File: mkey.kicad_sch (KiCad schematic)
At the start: 161 parts, among them J1 USB_C_REP_2.0, SW1 SW_Push, SW2 SW_Push, U1 ESP32-S3-WROOM-1, U5 SY8088

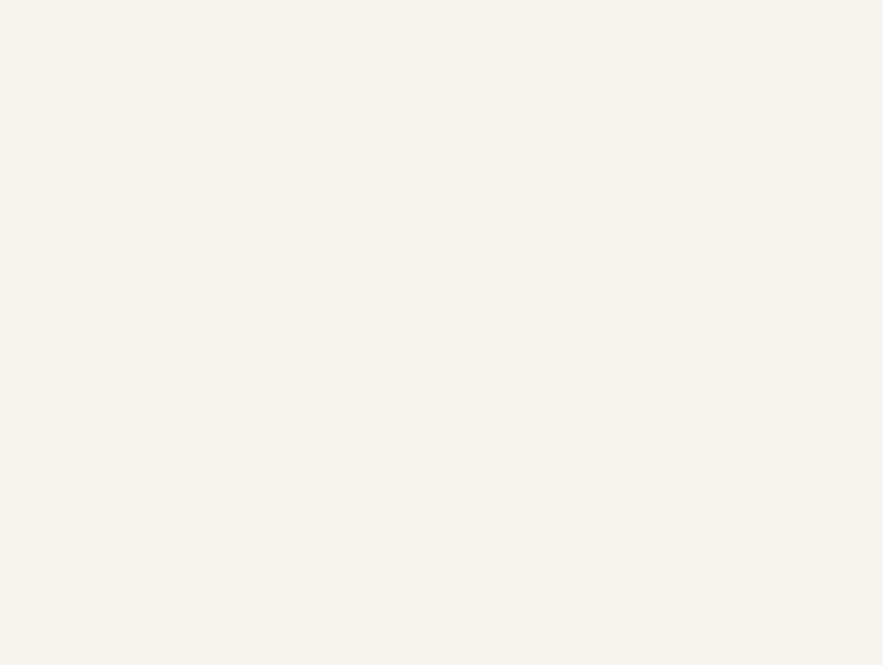
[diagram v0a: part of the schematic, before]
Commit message: Add display connector to schematic, thicken power traces
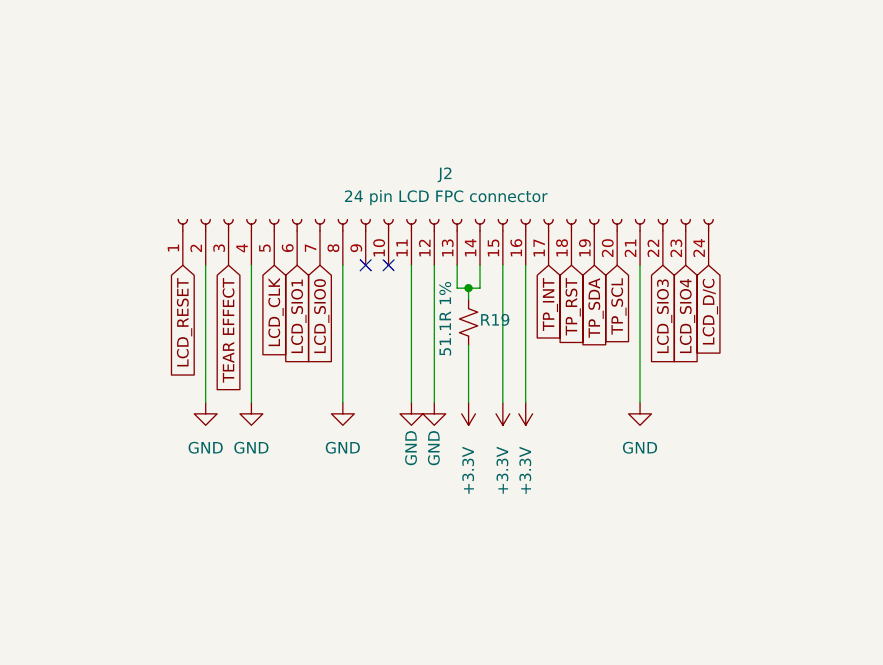
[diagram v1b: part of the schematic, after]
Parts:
- added J2: 24 pin LCD FPC connector, CONN-SMD_24P-P0.40__X0400FVS-24-LPSN:CONN-SMD_24P-P0.40_X0400FVS-24-LPSN, symbol Connector:Conn_01x24_Socket
- added R19: 51.1R 1%, Resistor_SMD:R_0603_1608Metric, symbol Device:R_Small_US
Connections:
- net GND: now also J2.11 (Pin_11), J2.12 (Pin_12), J2.2 (Pin_2), J2.21 (Pin_21), J2.4 (Pin_4), J2.8 (Pin_8)
- new net: J2.13 (Pin_13), J2.14 (Pin_14), R19.1
- new net +3.3V: J2.15 (Pin_15), J2.16 (Pin_16), R19.2
- new net LCD_CLK: J2.5 (Pin_5)
- new net LCD_D/C: J2.24 (Pin_24)
- new net LCD_RESET: J2.1 (Pin_1)
- new net LCD_SIO0: J2.7 (Pin_7)
- new net LCD_SIO1: J2.6 (Pin_6)
- new net LCD_SIO3: J2.22 (Pin_22)
- new net LCD_SIO4: J2.23 (Pin_23)
- new net TEAR EFFECT: J2.3 (Pin_3)
- new net TP_INT: J2.17 (Pin_17)
- new net TP_RST: J2.18 (Pin_18)
- new net TP_SCL: J2.20 (Pin_20)
- new net TP_SDA: J2.19 (Pin_19)
- no-connect marks 2 -> 4

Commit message: edit connector symbol to layout pins linearly, update pcb
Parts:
- J2: footprint CONN-SMD_24P-P0.40__X0400FVS-24-LPSN:CONN-SMD_24P-P0.40_X0400FVS-24-LPSN -> CONN-SMD_24P-P0.40_X0400FVS-24-LPSN-LINEAR:CONN-SMD_24P-P0.40_X0400FVS-24-LPSN-LINEAR
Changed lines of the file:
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@@
       (effects (font (size 1.27 1.27)))
     )
-    (property "Footprint" "CONN-SMD_24P-P0.40__X0400FVS-24-LPSN:CONN-SMD_24P-P0.40_X0400FVS-24-LPSN" (at 294.64 203.2 0)
+    (property "Footprint" "CONN-SMD_24P-P0.40_X0400FVS-24-LPSN-LINEAR:CONN-SMD_24P-P0.40_X0400FVS-24-LPSN-LINEAR" (at 294.64 203.2 0)
       (effects (font (size 1.27 1.27)) hide)
     )

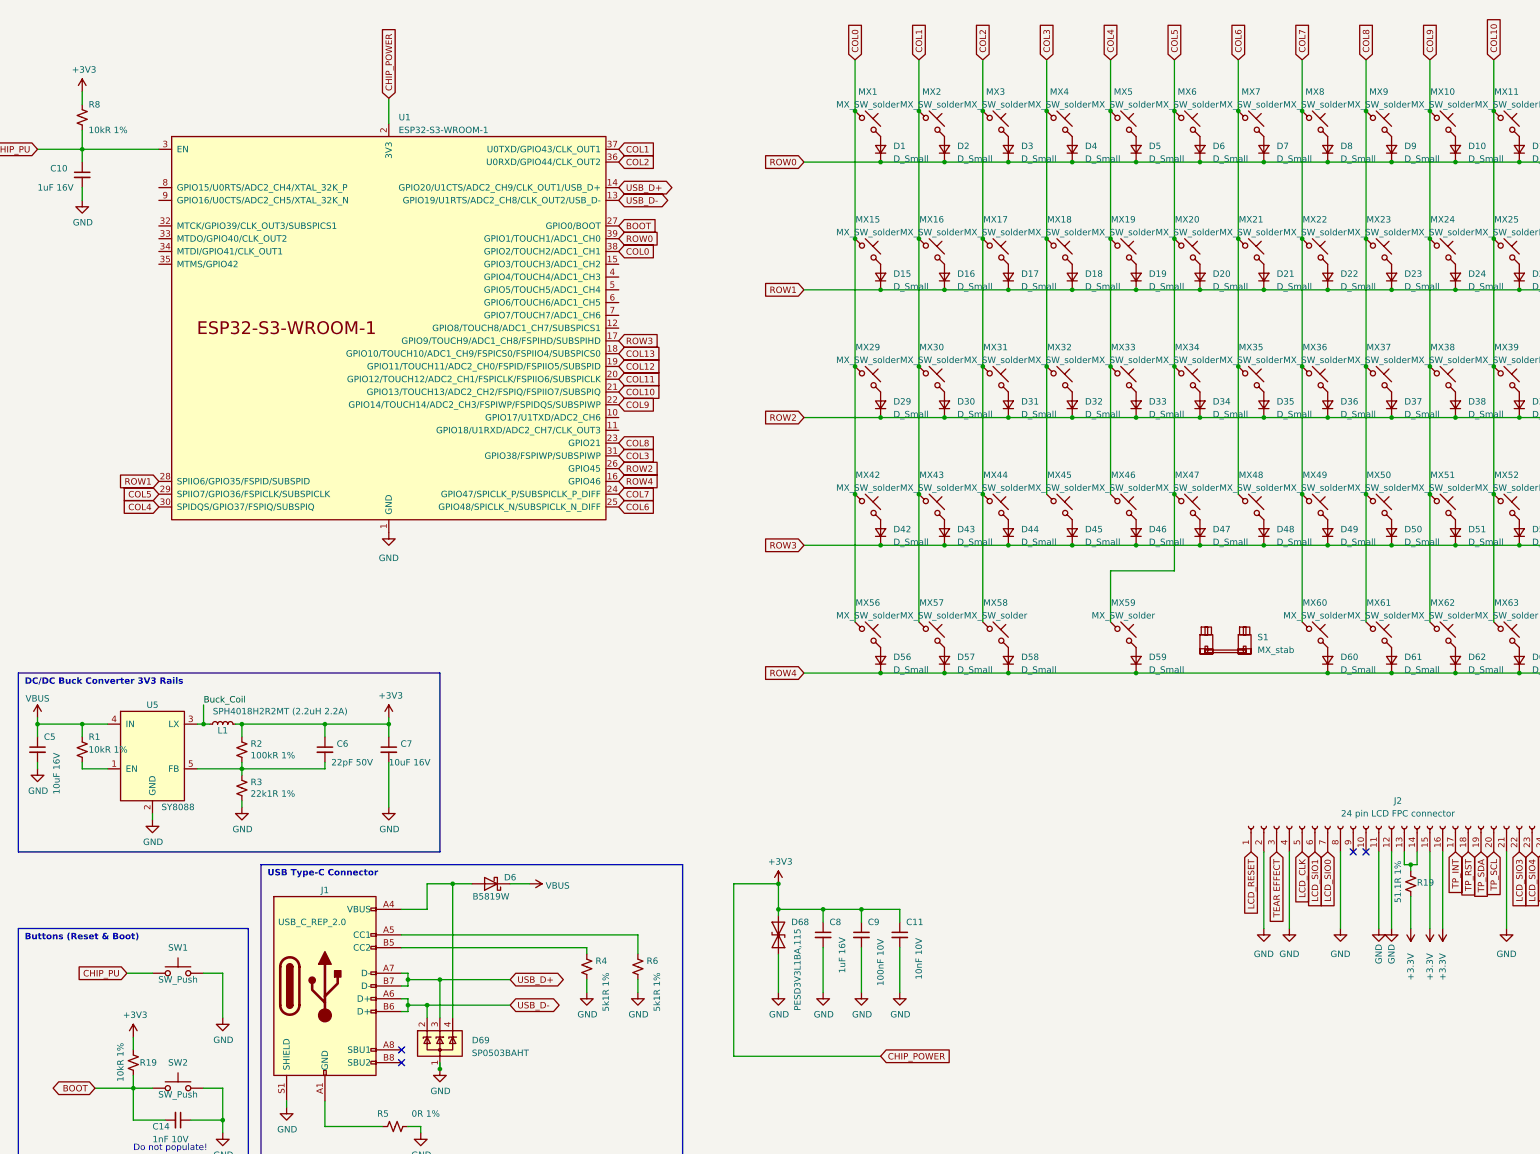
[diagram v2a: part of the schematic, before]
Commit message: Added display silk and connector. Began routing of connector. Dropped support for external jtag
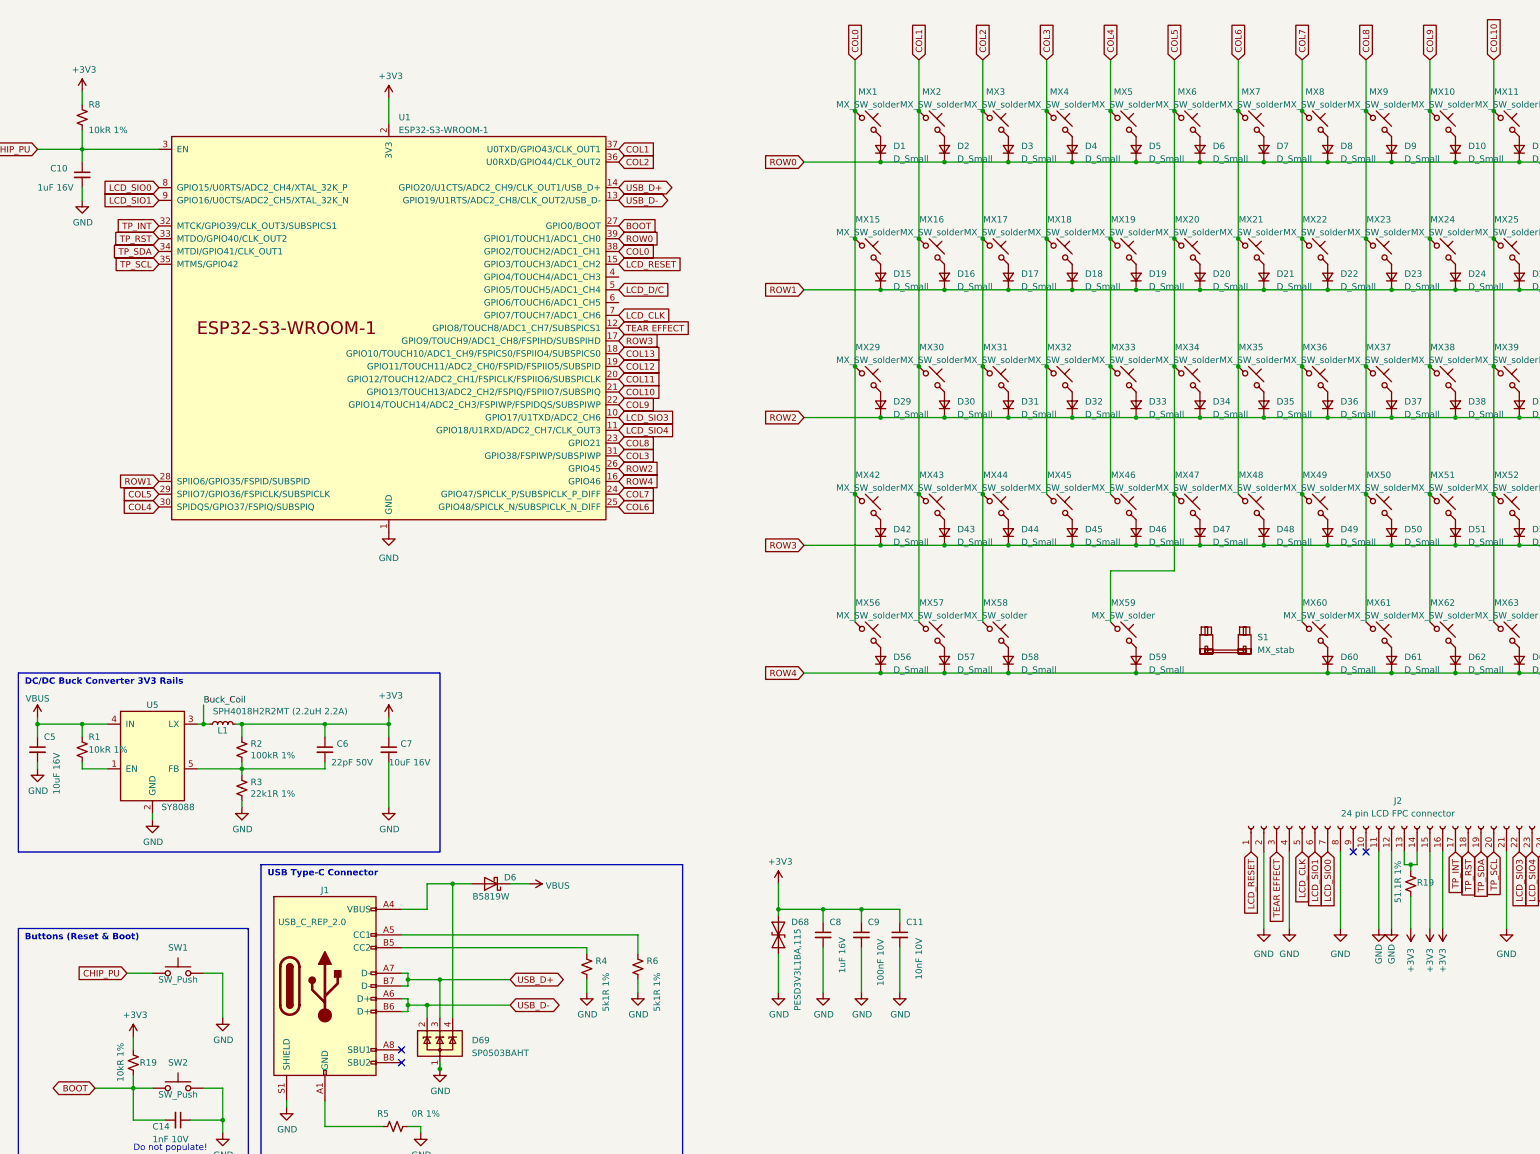
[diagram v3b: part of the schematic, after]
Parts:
- J2: footprint CONN-SMD_24P-P0.40_X0400FVS-24-LPSN-LINEAR:CONN-SMD_24P-P0.40_X0400FVS-24-LPSN-LINEAR -> 24P_LCD_CONN:CONN-SMD_24P-P0.40_X0400FVS-24-LPSN-LINEAR
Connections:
- net +3.3V is gone; now on net +3V3: J2.15 (Pin_15), J2.16 (Pin_16), R19.2
- net LCD_CLK: now also U1.7 (GPIO7/TOUCH7/ADC1_CH6)
- net LCD_D/C: now also U1.5 (GPIO5/TOUCH5/ADC1_CH4)
- net LCD_RESET: now also U1.15 (GPIO3/TOUCH3/ADC1_CH2)
- net LCD_SIO0: now also U1.8 (GPIO15/U0RTS/ADC2_CH4/XTAL_32K_P)
- net LCD_SIO1: now also U1.9 (GPIO16/U0CTS/ADC2_CH5/XTAL_32K_N)
- net LCD_SIO3: now also U1.10 (GPIO17/U1TXD/ADC2_CH6)
- net LCD_SIO4: now also U1.11 (GPIO18/U1RXD/ADC2_CH7/CLK_OUT3)
- net TEAR EFFECT: now also U1.12 (GPIO8/TOUCH8/ADC1_CH7/SUBSPICS1)
- net TP_INT: now also U1.32 (MTCK/GPIO39/CLK_OUT3/SUBSPICS1)
- net TP_RST: now also U1.33 (MTDO/GPIO40/CLK_OUT2)
- net TP_SCL: now also U1.35 (MTMS/GPIO42)
- net TP_SDA: now also U1.34 (MTDI/GPIO41/CLK_OUT1)

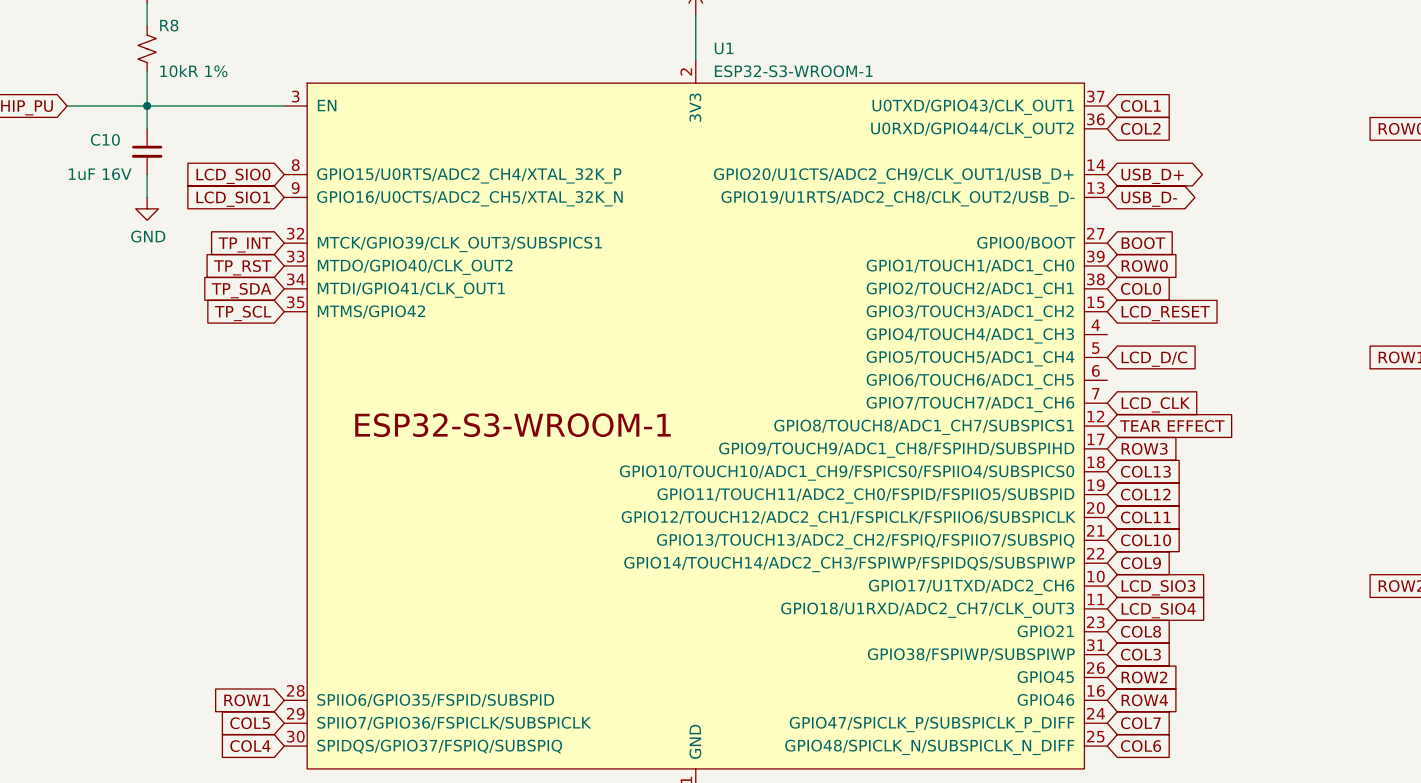
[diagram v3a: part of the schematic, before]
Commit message: Routed display connector, now to DRC it and triple check
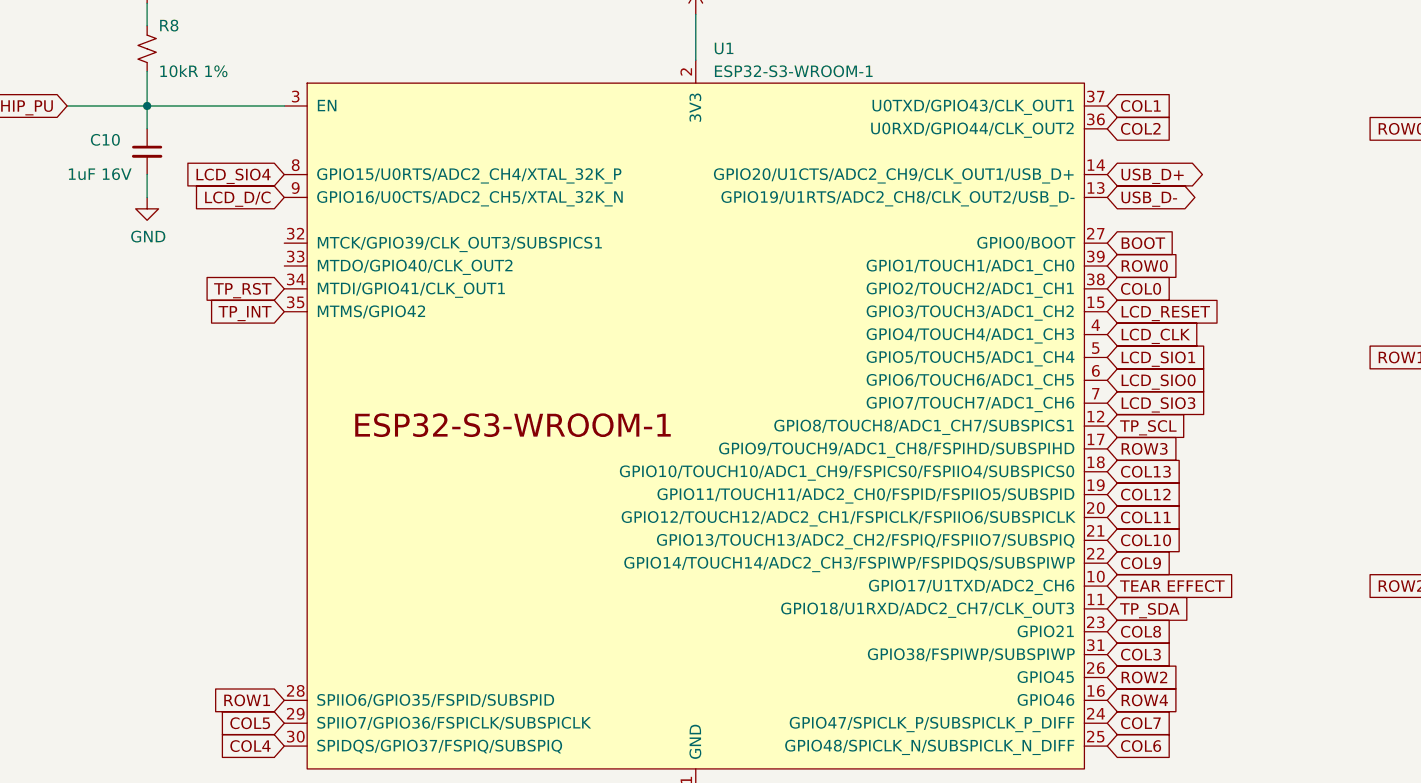
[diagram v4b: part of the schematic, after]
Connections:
- net LCD_CLK: now also U1.4 (GPIO4/TOUCH4/ADC1_CH3); no longer U1.7 (GPIO7/TOUCH7/ADC1_CH6)
- net LCD_D/C: now also U1.9 (GPIO16/U0CTS/ADC2_CH5/XTAL_32K_N); no longer U1.5 (GPIO5/TOUCH5/ADC1_CH4)
- net LCD_SIO0: now also U1.6 (GPIO6/TOUCH6/ADC1_CH5); no longer U1.8 (GPIO15/U0RTS/ADC2_CH4/XTAL_32K_P)
- net LCD_SIO1: now also U1.5 (GPIO5/TOUCH5/ADC1_CH4); no longer U1.9 (GPIO16/U0CTS/ADC2_CH5/XTAL_32K_N)
- net LCD_SIO3: now also U1.7 (GPIO7/TOUCH7/ADC1_CH6); no longer U1.10 (GPIO17/U1TXD/ADC2_CH6)
- net LCD_SIO4: now also U1.8 (GPIO15/U0RTS/ADC2_CH4/XTAL_32K_P); no longer U1.11 (GPIO18/U1RXD/ADC2_CH7/CLK_OUT3)
- net TEAR EFFECT: now also U1.10 (GPIO17/U1TXD/ADC2_CH6); no longer U1.12 (GPIO8/TOUCH8/ADC1_CH7/SUBSPICS1)
- net TP_INT: now also U1.35 (MTMS/GPIO42); no longer U1.32 (MTCK/GPIO39/CLK_OUT3/SUBSPICS1)
- net TP_RST: now also U1.34 (MTDI/GPIO41/CLK_OUT1); no longer U1.33 (MTDO/GPIO40/CLK_OUT2)
- net TP_SCL: now also U1.12 (GPIO8/TOUCH8/ADC1_CH7/SUBSPICS1); no longer U1.35 (MTMS/GPIO42)
- net TP_SDA: now also U1.11 (GPIO18/U1RXD/ADC2_CH7/CLK_OUT3); no longer U1.34 (MTDI/GPIO41/CLK_OUT1)

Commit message: vias, vias everywhere
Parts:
- C14: now not fitted
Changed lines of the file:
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@@
   )
   (symbol (lib_id "Device:C_Small") (at 53.34 261.62 270) (unit 1)
-    (in_bom no) (on_board yes) (dnp no)
+    (in_bom no) (on_board yes) (dnp yes)
     (property "Reference" "C14" (at 48.26 262.89 90)
       (effects (font (size 1.27 1.27)) (justify left))

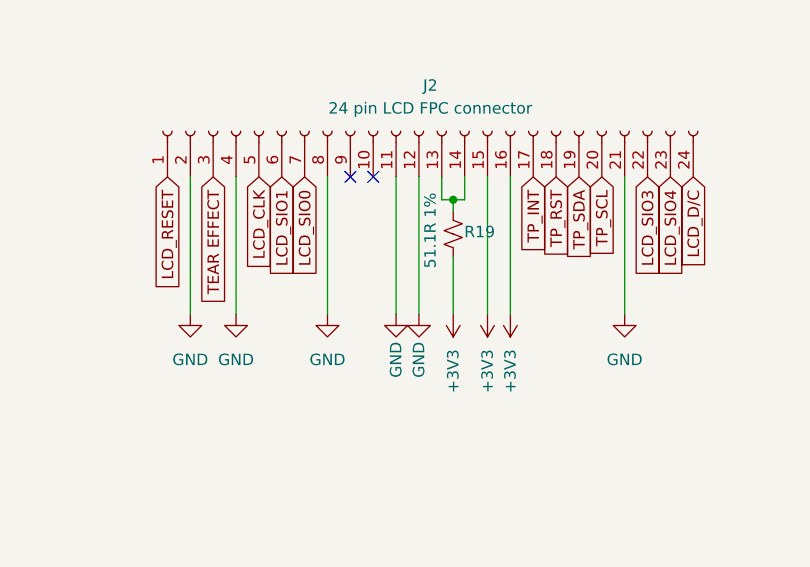
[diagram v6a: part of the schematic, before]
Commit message: Fix fpc connector schematic
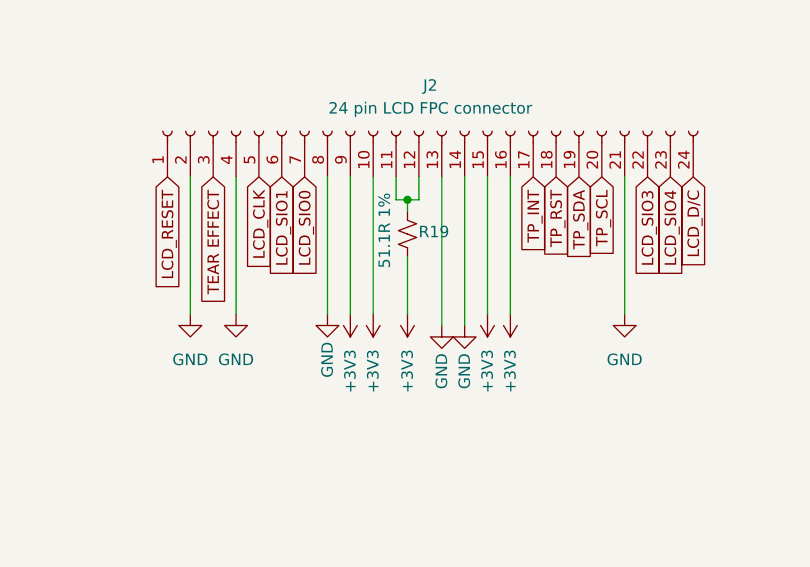
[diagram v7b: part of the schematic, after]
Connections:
- net +3V3: now also J2.10 (Pin_10), J2.9 (Pin_9)
- net GND: now also J2.13 (Pin_13), J2.14 (Pin_14); no longer J2.11 (Pin_11), J2.12 (Pin_12)
- new net: J2.11 (Pin_11), J2.12 (Pin_12), R19.1
- no-connect marks 4 -> 2
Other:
- moved on the sheet: R19
